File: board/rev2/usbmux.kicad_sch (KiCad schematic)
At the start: 7 parts, among them SW5 MS-22D28-G020, U17 TS3USB30ERSWR, U18 TS3USB30ERSWR

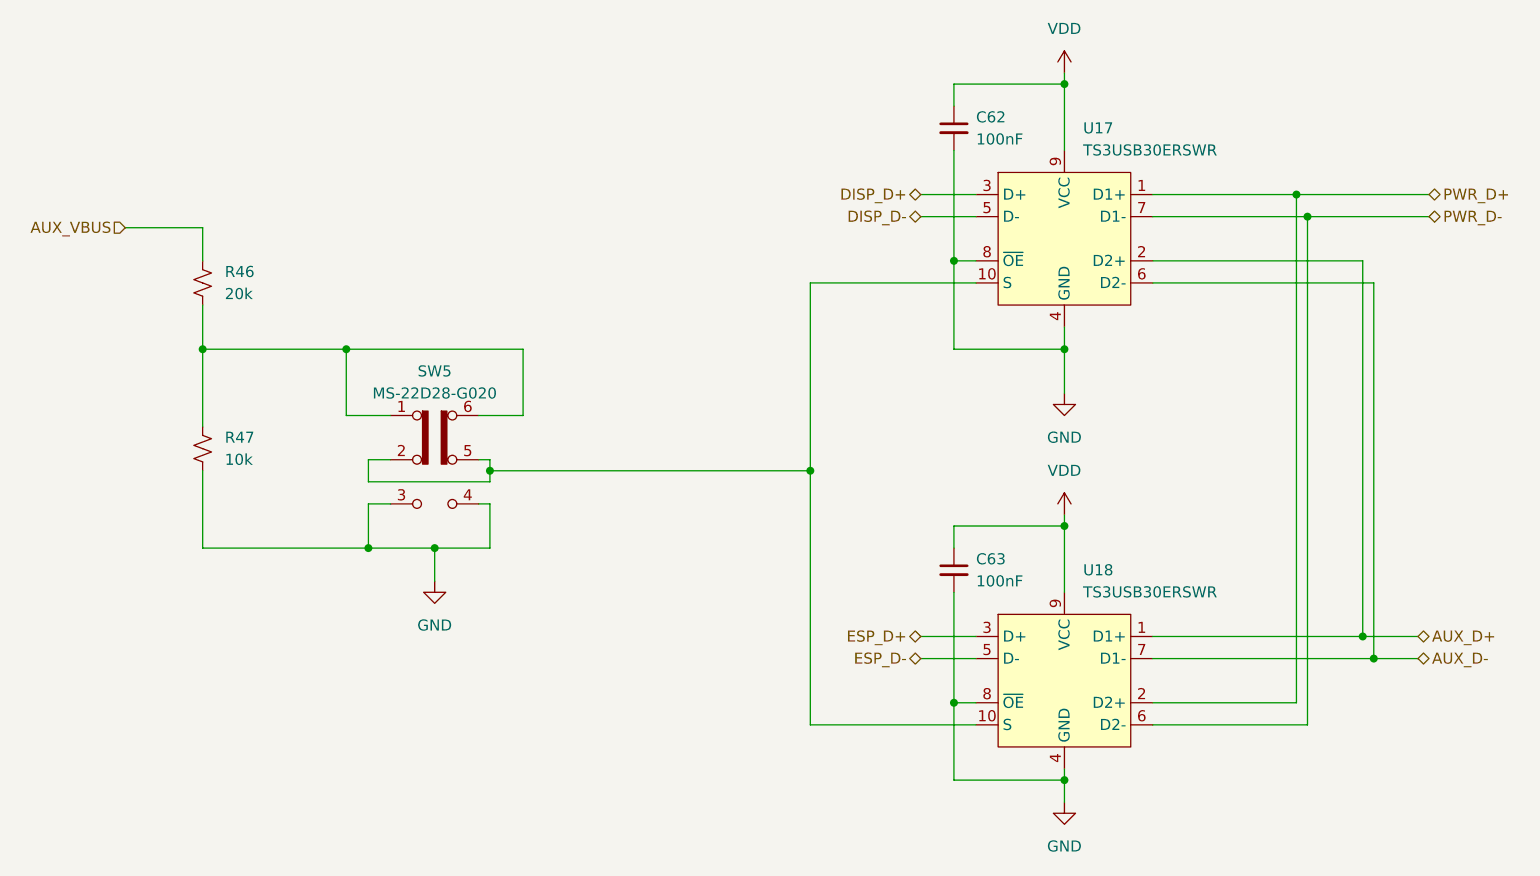
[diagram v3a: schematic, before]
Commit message: Start board
add a few extra bypass caps too, and swap some pins on the USB mux

i forgot to add a bypass cap on the tpd6s so that also needs to happen

truly 63 capacitors is not enough
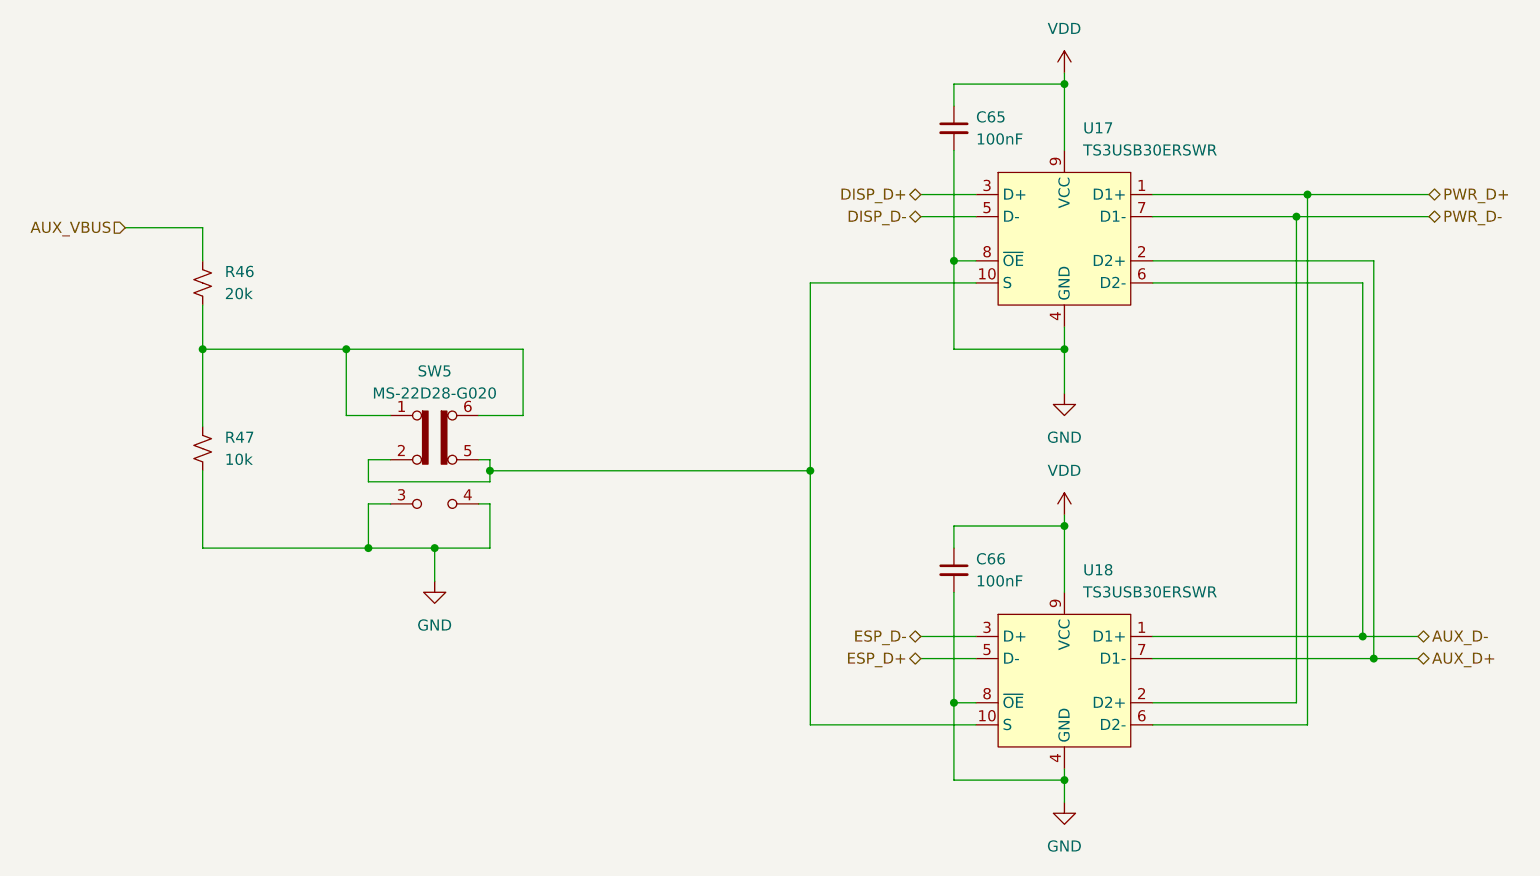
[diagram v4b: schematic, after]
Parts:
- renumbered C62 to C65, C63 to C66
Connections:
- net AUX_D+: now also U18.7 (D1-); no longer U18.1 (D1+)
- net AUX_D-: now also U18.1 (D1+); no longer U18.7 (D1-)
- net ESP_D+: now also U18.5 (D-); no longer U18.3 (D+)
- net ESP_D-: now also U18.3 (D+); no longer U18.5 (D-)
- net PWR_D+: now also U18.6 (D2-); no longer U18.2 (D2+)
- net PWR_D-: now also U18.2 (D2+); no longer U18.6 (D2-)
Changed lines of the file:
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@@
+	)
+	(junction
+		(at 198.12 69.85)
+		(diameter 0)
+		(color 0 0 0 0)
+	)
+	(junction
+		(at 196.85 72.39)
+		(diameter 0)
+		(color 0 0 0 0)
 	)
 	(junction
@@
 	)
 	(junction
-		(at 196.85 69.85)
-		(diameter 0)
-		(color 0 0 0 0)
-	)
-	(junction
 		(at 170.18 57.15)
 		(diameter 0)
@@
 	)
 	(junction
-		(at 198.12 72.39)
-		(diameter 0)
-		(color 0 0 0 0)
-	)
-	(junction
 		(at 90.17 110.49)
 		(diameter 0)
@@
 	(wire
 		(pts
+			(xy 196.85 72.39) (xy 212.09 72.39)
+		)
+		(stroke
+			(width 0)
+			(type default)
+		)
+	)
+	(wire
+		(pts
 			(xy 107.95 95.25) (xy 102.87 95.25)
 		)
@@
 	(wire
 		(pts
-			(xy 196.85 69.85) (xy 212.09 69.85)
+			(xy 180.34 69.85) (xy 198.12 69.85)
 		)
 		(stroke
@@
 	(wire
 		(pts
-			(xy 198.12 72.39) (xy 212.09 72.39)
+			(xy 198.12 69.85) (xy 198.12 130.81)
 		)
 		(stroke
@@
 	(wire
 		(pts
+			(xy 204.47 80.01) (xy 204.47 120.65)
+		)
+		(stroke
+			(width 0)
+			(type default)
+		)
+	)
+	(wire
+		(pts
 			(xy 62.23 73.66) (xy 71.12 73.66)
 		)
@@
 	(wire
 		(pts
-			(xy 180.34 80.01) (xy 205.74 80.01)
-		)
-		(stroke
-			(width 0)
-			(type default)
-		)
-	)
-	(wire
-		(pts
 			(xy 157.48 128.27) (xy 157.48 137.16)
 		)
@@
 	(wire
 		(pts
+			(xy 196.85 72.39) (xy 196.85 128.27)
+		)
+		(stroke
+			(width 0)
+			(type default)
+		)
+	)
+	(wire
+		(pts
 			(xy 71.12 73.66) (xy 71.12 77.47)
 		)
@@
 	(wire
 		(pts
+			(xy 205.74 77.47) (xy 205.74 123.19)
+		)
+		(stroke
+			(width 0)
+			(type default)
+		)
+	)
+	(wire
+		(pts
 			(xy 102.87 105.41) (xy 104.14 105.41)
 		)
@@
 	(wire
 		(pts
+			(xy 204.47 80.01) (xy 180.34 80.01)
+		)
+		(stroke
+			(width 0)
+			(type default)
+		)
+	)
+	(wire
+		(pts
 			(xy 153.67 72.39) (xy 160.02 72.39)
 		)
@@
 	(wire
 		(pts
-			(xy 180.34 72.39) (xy 198.12 72.39)
-		)
-		(stroke
-			(width 0)
-			(type default)
-		)
-	)
-	(wire
-		(pts
-			(xy 198.12 130.81) (xy 198.12 72.39)
-		)
-		(stroke
-			(width 0)
-			(type default)
-		)
-	)
-	(wire
-		(pts
-			(xy 180.34 69.85) (xy 196.85 69.85)
+			(xy 180.34 72.39) (xy 196.85 72.39)
 		)
 		(stroke
@@
 	(wire
 		(pts
-			(xy 180.34 77.47) (xy 204.47 77.47)
-		)
-		(stroke
-			(width 0)
-			(type default)
-		)
-	)
-	(wire
-		(pts
 			(xy 140.97 80.01) (xy 160.02 80.01)
 		)
@@
 	(wire
 		(pts
-			(xy 196.85 128.27) (xy 196.85 69.85)
-		)
-		(stroke
-			(width 0)
-			(type default)
-		)
-	)
-	(wire
-		(pts
-			(xy 205.74 80.01) (xy 205.74 123.19)
-		)
-		(stroke
-			(width 0)
-			(type default)
-		)
-	)
-	(wire
-		(pts
 			(xy 170.18 107.95) (xy 170.18 115.57)
 		)
@@
 	(wire
 		(pts
+			(xy 205.74 77.47) (xy 180.34 77.47)
+		)
+		(stroke
+			(width 0)
+			(type default)
+		)
+	)
+	(wire
+		(pts
 			(xy 71.12 101.6) (xy 71.12 110.49)
 		)
@@
 	(wire
 		(pts
+			(xy 198.12 69.85) (xy 212.09 69.85)
+		)
+		(stroke
+			(width 0)
+			(type default)
+		)
+	)
+	(wire
+		(pts
 			(xy 90.17 102.87) (xy 104.14 102.87)
-		)
-		(stroke
-			(width 0)
-			(type default)
-		)
-	)
-	(wire
-		(pts
-			(xy 204.47 77.47) (xy 204.47 120.65)
 		)
 		(stroke
@@
 	(hierarchical_label "AUX_D+"
 		(shape bidirectional)
+		(at 210.82 123.19 0)
+		(effects
+			(font
+				(size 1.27 1.27)
+			)
+			(justify left)
+		)
+	)
+	(hierarchical_label "AUX_D-"
+		(shape bidirectional)
 		(at 210.82 120.65 0)
 		(effects
@@
 		)
 	)
-	(hierarchical_label "AUX_D-"
-		(shape bidirectional)
-		(at 210.82 123.19 0)
-		(effects
-			(font
-				(size 1.27 1.27)
-			)
-			(justify left)
-		)
-	)
 	(hierarchical_label "ESP_D-"
 		(shape bidirectional)
-		(at 153.67 123.19 180)
+		(at 153.67 120.65 180)
 		(effects
 			(font
@@
 	(hierarchical_label "ESP_D+"
 		(shape bidirectional)
-		(at 153.67 120.65 180)
+		(at 153.67 123.19 180)
 		(effects
 			(font
@@
 		(dnp no)
 		(fields_autoplaced yes)
-		(property "Reference" "#PWR062"
+		(property "Reference" "#PWR063"
 			(at 170.18 146.05 0)
 			(effects
@@
 			(project ""
 				(path "/32eb05c7-b4a6-42f3-8fb3-43453631100f/f949a322-cdc0-42f3-8e56-a599c8860839"
-					(reference "#PWR062")
+					(reference "#PWR063")
 					(unit 1)
 				)
@@
 		(dnp no)
 		(fields_autoplaced yes)
-		(property "Reference" "#PWR058"
+		(property "Reference" "#PWR059"
 			(at 97.79 120.65 0)
 			(effects
@@
 			(project ""
 				(path "/32eb05c7-b4a6-42f3-8fb3-43453631100f/f949a322-cdc0-42f3-8e56-a599c8860839"
-					(reference "#PWR058")
+					(reference "#PWR059")
 					(unit 1)
 				)
@@
 		(dnp no)
 		(fields_autoplaced yes)
-		(property "Reference" "C63"
+		(property "Reference" "C66"
 			(at 160.02 111.7662 0)
 			(effects
@@
 			(project "mainboard"
 				(path "/32eb05c7-b4a6-42f3-8fb3-43453631100f/f949a322-cdc0-42f3-8e56-a599c8860839"
-					(reference "C63")
+					(reference "C66")
 					(unit 1)
 				)
@@
 		(dnp no)
 		(fields_autoplaced yes)
-		(property "Reference" "#PWR060"
+		(property "Reference" "#PWR061"
 			(at 170.18 99.06 0)
 			(effects
@@
 			(project ""
 				(path "/32eb05c7-b4a6-42f3-8fb3-43453631100f/f949a322-cdc0-42f3-8e56-a599c8860839"
-					(reference "#PWR060")
+					(reference "#PWR061")
 					(unit 1)
 				)
@@
 		(dnp no)
 		(fields_autoplaced yes)
-		(property "Reference" "C62"
+		(property "Reference" "C65"
 			(at 160.02 60.9662 0)
 			(effects
@@
 			(project ""
 				(path "/32eb05c7-b4a6-42f3-8fb3-43453631100f/f949a322-cdc0-42f3-8e56-a599c8860839"
-					(reference "C62")
+					(reference "C65")
 					(unit 1)
 				)
@@
 		(dnp no)
 		(fields_autoplaced yes)
-		(property "Reference" "#PWR061"
+		(property "Reference" "#PWR062"
 			(at 170.18 110.49 0)
 			(effects
@@
 			(project "mainboard"
 				(path "/32eb05c7-b4a6-42f3-8fb3-43453631100f/f949a322-cdc0-42f3-8e56-a599c8860839"
-					(reference "#PWR061")
+					(reference "#PWR062")
 					(unit 1)
 				)
@@
 		(dnp no)
 		(fields_autoplaced yes)
-		(property "Reference" "#PWR059"
+		(property "Reference" "#PWR060"
 			(at 170.18 59.69 0)
 			(effects
@@
 			(project ""
 				(path "/32eb05c7-b4a6-42f3-8fb3-43453631100f/f949a322-cdc0-42f3-8e56-a599c8860839"
-					(reference "#PWR059")
+					(reference "#PWR060")
 					(unit 1)
 				)

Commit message: Finish board rev2
woo another pcb
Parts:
- SW5: value MS-22D28-G020 -> MS-22D17AG2.5-B; footprint Switch_Slide_SMD:SW-SMD_MS-22D28-G020 -> Switch_Slide_SMD:SW-SMD_MS-22D17AG2.5; LCSC C963205 -> C20611671; Part MS-22D28-G020 -> MS-22D17AG2.5-B
